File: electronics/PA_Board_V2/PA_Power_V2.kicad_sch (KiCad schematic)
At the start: 36 parts, among them J4 Conn_01x02, Q1 AOD4185, U10 INA219AxD, U11 TLV70233, U6 LMR51420, U7 MCP4725, U9 AP2204K-ADJ

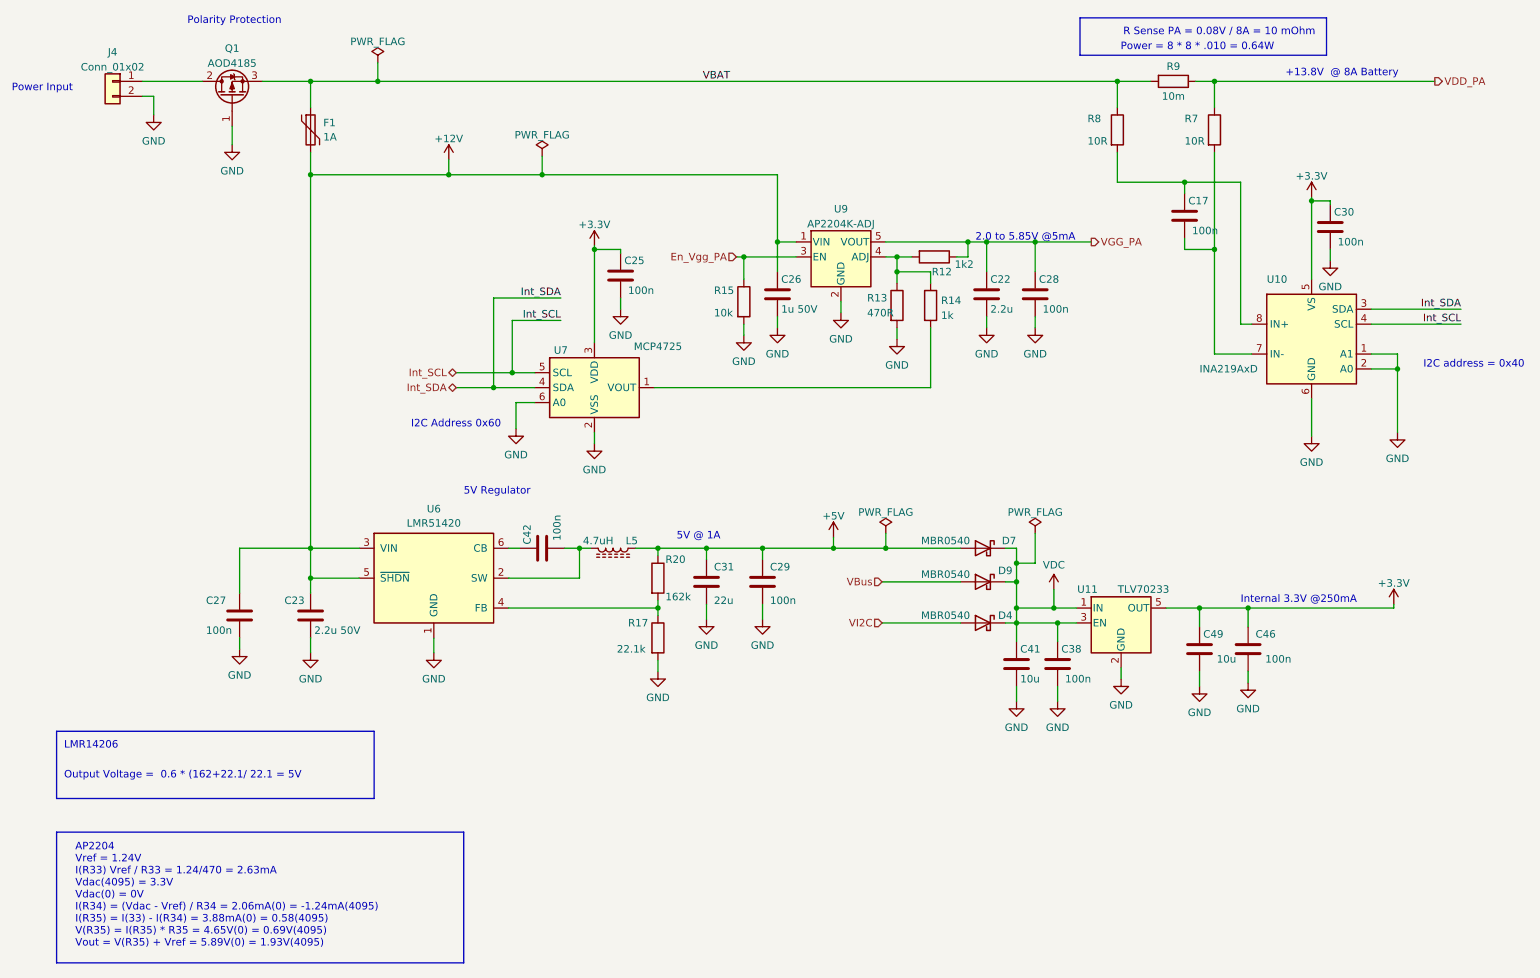
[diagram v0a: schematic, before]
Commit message: Update Arduino documentation and change to Kicad V8
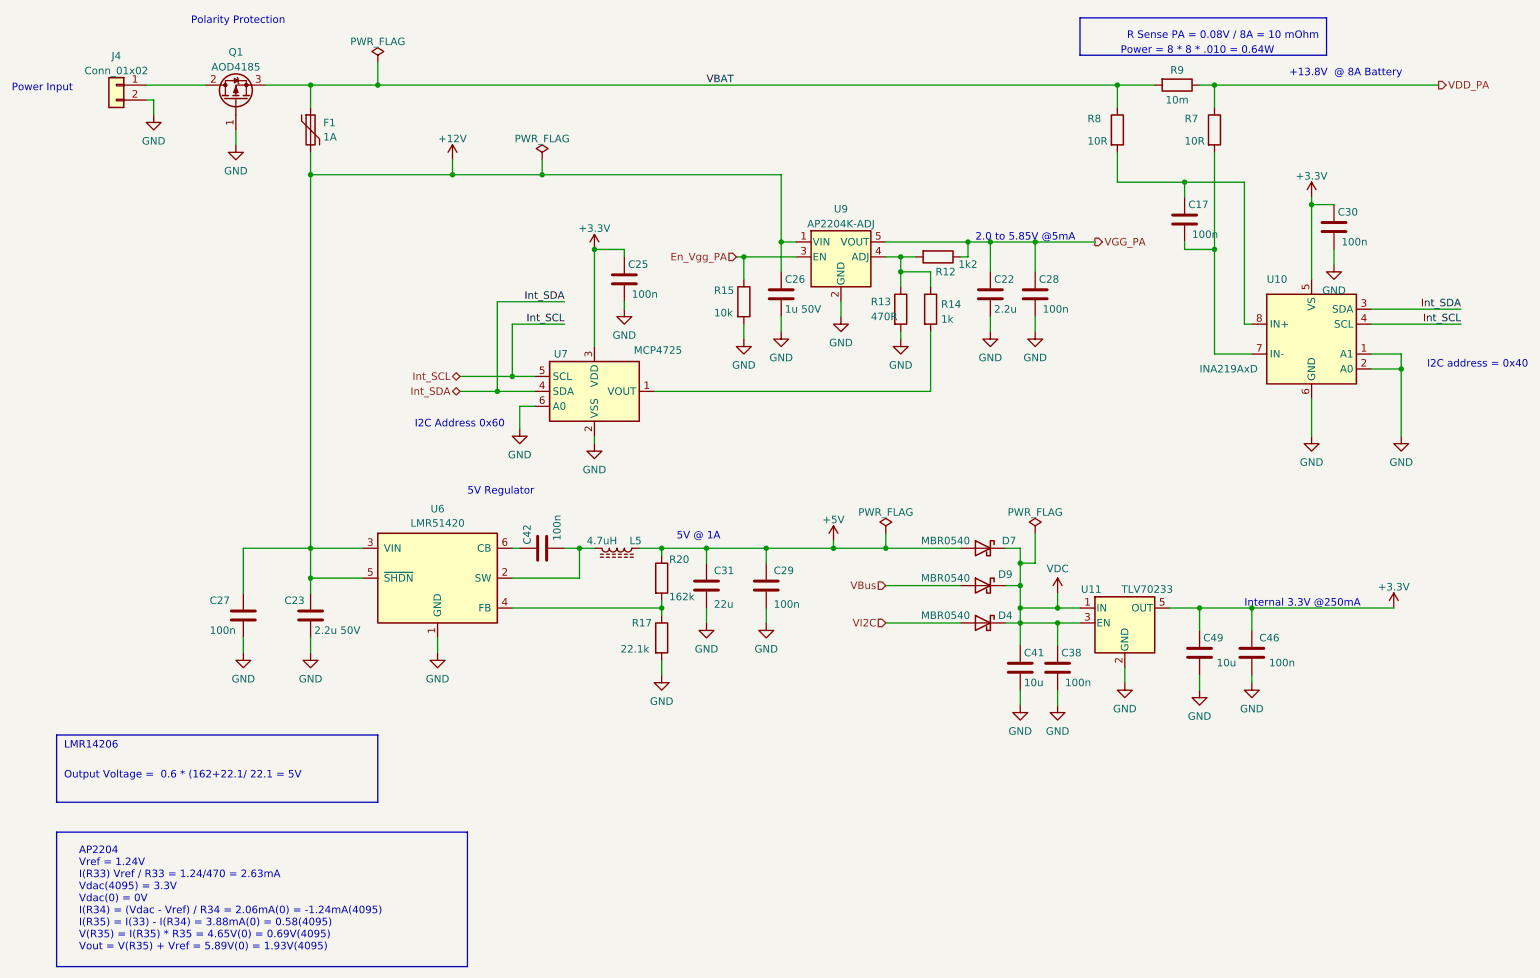
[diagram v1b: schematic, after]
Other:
- moved on the sheet: C17, C22, C25, C26, C27, C29, C30, C31, C38, C41, C46, C49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
